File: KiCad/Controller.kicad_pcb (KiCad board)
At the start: 2 copper layers, 45 x 45 mm, 37 parts, among them J1 Inputs, J2 POWER, J3 RANGER, J4 RFID, J5 OUT1, J6 OUT2, J7 OUT3, J8 OUT4, J9 USB-C, M1 D24V5F3-NoSHDN, M2 D24V5F5-NoSHDN, Q1 BC817, U1 ESP32-WROOM-32, U2 G3VM-41GR8, U3 G3VM-41GR8, U4 G3VM-41GR8, U5 G3VM-41GR8, U6 FT231XQ, U7 QR

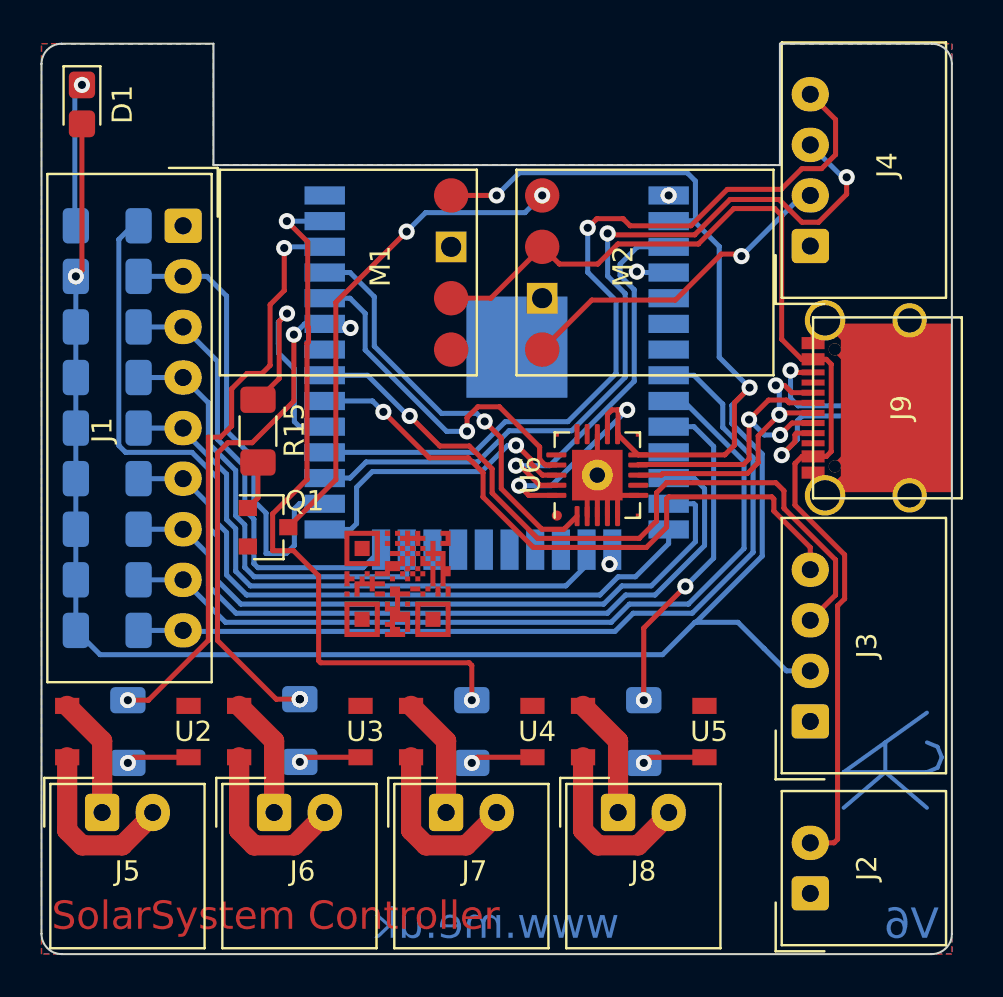
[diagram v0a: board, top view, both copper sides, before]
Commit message: Updated QR, and added 3D (not finished)
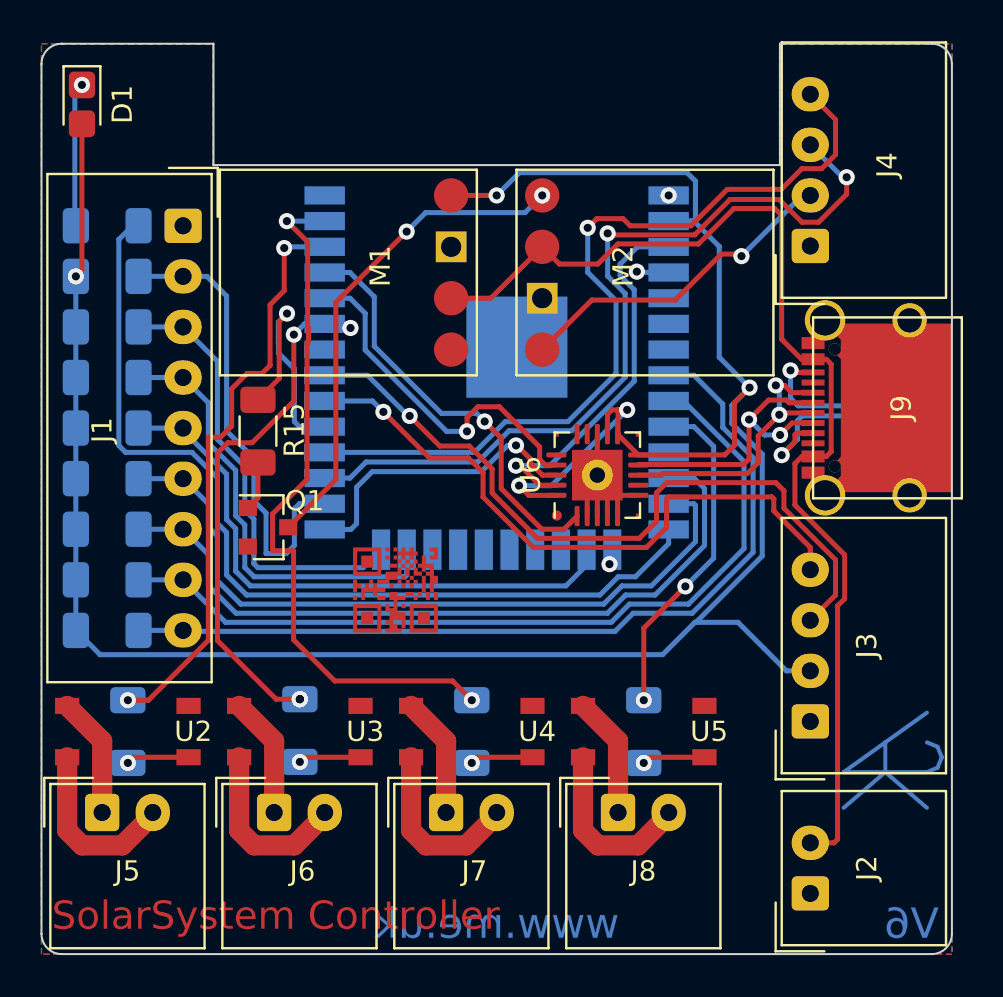
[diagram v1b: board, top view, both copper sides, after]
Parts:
- moved U7 0.32 mm to (67.5, 122.0)
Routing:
- net OUT3: track 35.7 -> 34.8 mm

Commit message: New regulator
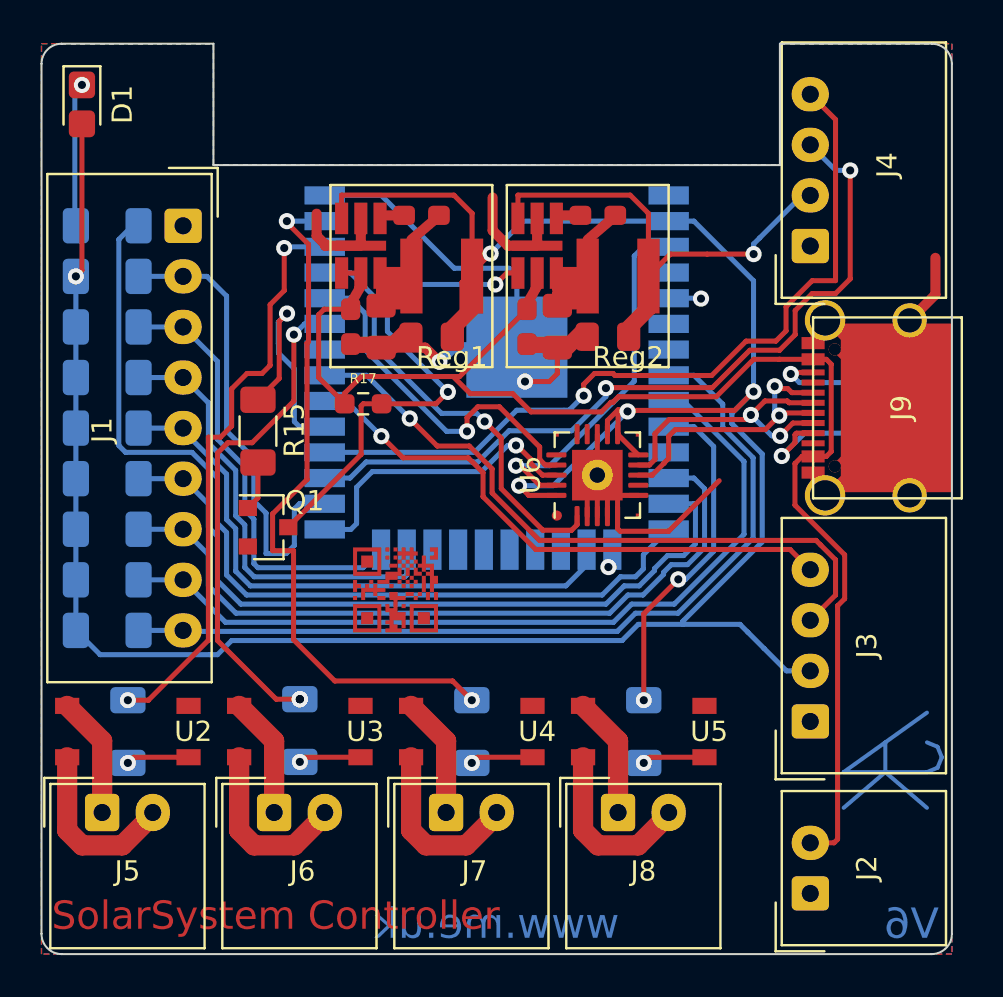
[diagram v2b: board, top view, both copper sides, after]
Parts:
- removed M1: D24V5F3-NoSHDN, RevK:D24V5F3-SMD-Like
- removed M2: D24V5F5-NoSHDN, RevK:D24V5F3-SMD-Like
- added R17: 100K, Resistor_SMD:R_0603_1608Metric_Pad0.98x0.95mm_HandSolder, F.Cu at (65.9, 112.8)
- added Reg1: Regulator, RevK:RegulatorBlock, F.Cu at (65.8, 105.0)
- added Reg2: Regulator, RevK:RegulatorBlock, F.Cu at (74.5, 105.0)
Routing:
- net GND: track 46.2 -> 100.5 mm, vias 3 -> 4
- net VBUS: track 55.6 -> 70.9 mm
- net SDA: track 32.0 -> 28.2 mm
- net SCL: track 36.8 -> 33.2 mm
- net +5V: track 16.5 -> 13.3 mm
- net +3V3: track 125.9 -> 123.1 mm
- net RFRX: track 41.3 -> 38.9 mm
- net Net-(J9-PadB5): track 7.07 -> 5.02 mm
- net RFTX: track 41.3 -> 39.6 mm
- net OUT2: track 25.9 -> 24.4 mm, vias 4 -> 3
- net Net-(J9-PadA5): track 8.07 -> 6.88 mm
- net EN: track 18.8 -> 18.1 mm
- net Net-(Q1-Pad3): track 24.5 -> 25.1 mm

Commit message: Yet more component tweaks
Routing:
- net GND: track 100.5 -> 107.4 mm, vias 4 -> 5
- net +3V3: track 123.1 -> 126.3 mm
- net +5V: track 13.3 -> 16.1 mm
- net VBUS: track 70.9 -> 71.5 mm

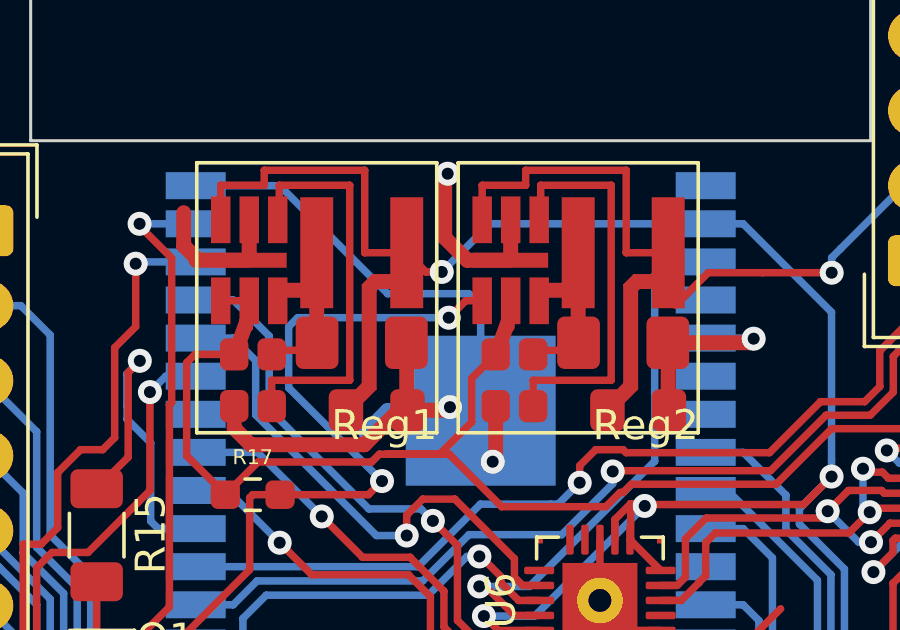
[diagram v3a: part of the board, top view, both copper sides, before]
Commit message: Cleaner regulator layout
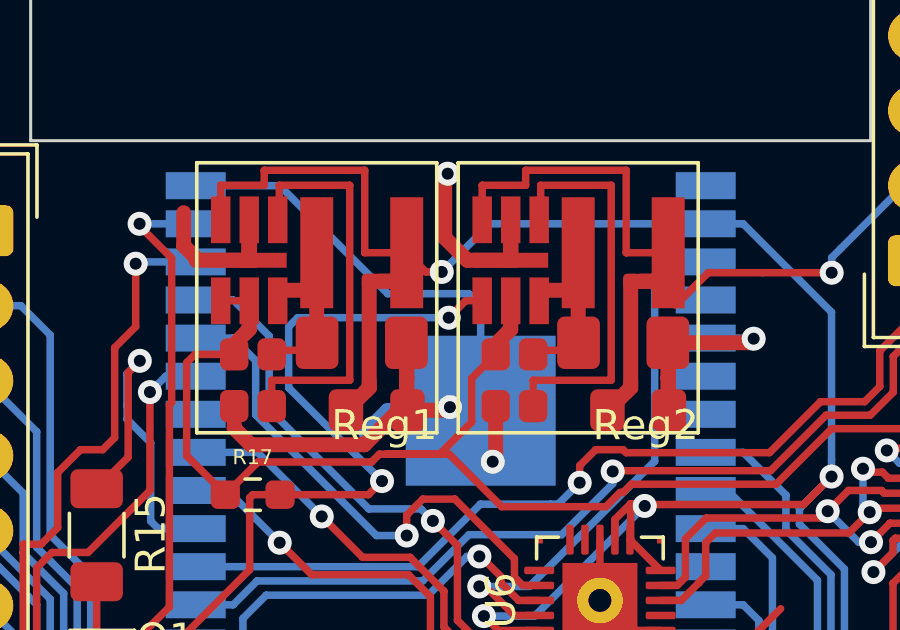
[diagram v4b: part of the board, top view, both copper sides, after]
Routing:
- net GND: track 107.4 -> 101.4 mm
- net +3V3: track 126.3 -> 120.5 mm
- net +5V: track 16.1 -> 10.9 mm
- net VBUS: track 71.5 -> 67.5 mm

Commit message: Yet more tweaks!
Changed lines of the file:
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@@
       (effects (font (size 1 1) (thickness 0.15)))
     )
+    (fp_line (start 0.75 4.75) (end 0.75 4) (layer F.Cu) (width 0.25))
+    (fp_line (start 0.5 -3) (end 3.85 -3) (layer F.Cu) (width 0.25))
+    (fp_line (start -0.95 -1.3) (end -0.95 -2.5) (layer F.Cu) (width 0.25))
+    (fp_line (start 1 -2.5) (end 3.35 -2.5) (layer F.Cu) (width 0.25))
+    (fp_line (start 1 -1.3) (end 1 -2.5) (layer F.Cu) (width 0.25))
+    (fp_line (start 3.35 4) (end 3.35 -2.5) (layer F.Cu) (width 0.25))
+    (fp_line (start 0.75 4) (end 3.35 4) (layer F.Cu) (width 0.25))
+    (fp_line (start 2.25 3) (end 0.75 3) (layer F.Cu) (width 0.25))
+    (fp_line (start 2.25 1) (end 2.25 3) (layer F.Cu) (width 0.5))
+    (fp_line (start 2.4 1) (end 1 1) (layer F.Cu) (width 0.5))
+    (fp_line (start -1.75 5.75) (end -1.75 -3.25) (layer F.Fab) (width 0.12))
+    (fp_line (start 6.25 5.75) (end -1.75 5.75) (layer F.Fab) (width 0.12))
+    (fp_line (start 6.25 -3.25) (end 6.25 5.75) (layer F.Fab) (width 0.12))
+    (fp_line (start -1.75 -3.25) (end 6.25 -3.25) (layer F.Fab) (width 0.12))
+    (fp_line (start -1.75 5.75) (end -1.75 -3.25) (layer F.CrtYd) (width 0.12))
+    (fp_line (start 6.25 5.75) (end -1.75 5.75) (layer F.CrtYd) (width 0.12))
+    (fp_line (start 6.25 -3.25) (end 6.25 5.75) (layer F.CrtYd) (width 0.12))
+    (fp_line (start -1.75 -3.25) (end 6.25 -3.25) (layer F.CrtYd) (width 0.12))
+    (fp_line (start -1.75 5.75) (end -1.75 -3.25) (layer F.SilkS) (width 0.12))
+    (fp_line (start 6.25 5.75) (end -1.75 5.75) (layer F.SilkS) (width 0.12))
+    (fp_line (start 6.25 -3.25) (end 6.25 5.75) (layer F.SilkS) (width 0.12))
+    (fp_line (start -1.75 -3.25) (end 6.25 -3.25) (layer F.SilkS) (width 0.12))
+    (fp_line (start 3.85 -0.25) (end 3.85 -3) (layer F.Cu) (width 0.25))
+    (fp_line (start 3.85 -0.25) (end 4.7 -0.25) (layer F.Cu) (width 0.25))
+    (fp_line (start 0.5 -2.5) (end 0.5 -3) (layer F.Cu) (width 0.25))
     (fp_line (start 0.5 -2.5) (end -0.95 -2.5) (layer F.Cu) (width 0.25))
-    (fp_line (start 0.5 -2.5) (end 0.5 -3) (layer F.Cu) (width 0.25))
-    (fp_line (start 3.85 -0.25) (end 4.7 -0.25) (layer F.Cu) (width 0.25))
-    (fp_line (start 3.85 -0.25) (end 3.85 -3) (layer F.Cu) (width 0.25))
-    (fp_line (start -1.75 -3.25) (end 6.25 -3.25) (layer F.SilkS) (width 0.12))
-    (fp_line (start 6.25 -3.25) (end 6.25 5.75) (layer F.SilkS) (width 0.12))
-    (fp_line (start 6.25 5.75) (end -1.75 5.75) (layer F.SilkS) (width 0.12))
-    (fp_line (start -1.75 5.75) (end -1.75 -3.25) (layer F.SilkS) (width 0.12))
-    (fp_line (start -1.75 -3.25) (end 6.25 -3.25) (layer F.CrtYd) (width 0.12))
-    (fp_line (start 6.25 -3.25) (end 6.25 5.75) (layer F.CrtYd) (width 0.12))
-    (fp_line (start 6.25 5.75) (end -1.75 5.75) (layer F.CrtYd) (width 0.12))
-    (fp_line (start -1.75 5.75) (end -1.75 -3.25) (layer F.CrtYd) (width 0.12))
-    (fp_line (start -1.75 -3.25) (end 6.25 -3.25) (layer F.Fab) (width 0.12))
-    (fp_line (start 6.25 -3.25) (end 6.25 5.75) (layer F.Fab) (width 0.12))
-    (fp_line (start 6.25 5.75) (end -1.75 5.75) (layer F.Fab) (width 0.12))
-    (fp_line (start -1.75 5.75) (end -1.75 -3.25) (layer F.Fab) (width 0.12))
-    (fp_line (start 2.4 1) (end 1 1) (layer F.Cu) (width 0.5))
-    (fp_line (start 2.25 1) (end 2.25 3) (layer F.Cu) (width 0.5))
-    (fp_line (start 2.25 3) (end 0.75 3) (layer F.Cu) (width 0.25))
-    (fp_line (start 0.75 4) (end 3.35 4) (layer F.Cu) (width 0.25))
-    (fp_line (start 3.35 4) (end 3.35 -2.5) (layer F.Cu) (width 0.25))
-    (fp_line (start 1 -1.3) (end 1 -2.5) (layer F.Cu) (width 0.25))
-    (fp_line (start 1 -2.5) (end 3.35 -2.5) (layer F.Cu) (width 0.25))
-    (fp_line (start -0.95 -1.3) (end -0.95 -2.5) (layer F.Cu) (width 0.25))
-    (fp_line (start 0.5 -3) (end 3.85 -3) (layer F.Cu) (width 0.25))
-    (fp_line (start 0.75 4.75) (end 0.75 4) (layer F.Cu) (width 0.25))
     (pad 4 smd rect (at 4.8 0.7 90) (size 0.5 1) (layers F.Cu)
       (net 17 +5V) (zone_connect 0))
@@
     (pad 2 smd rect (at 0 1.85) (size 0.5 1) (layers F.Cu)
       (net 18 VBUS) (zone_connect 0))
-    (pad 2 smd rect (at -0.3 2.6 135) (size 0.5 1) (layers F.Cu)
+    (pad 2 smd rect (at -0.35 2.65 135) (size 0.5 1) (layers F.Cu)
       (net 18 VBUS) (zone_connect 0))
     (pad 3 smd rect (at 5.25 4.35) (size 0.5 1) (layers F.Cu)
@@
       (effects (font (size 1 1) (thickness 0.15)))
     )
+    (fp_line (start 0.75 4.75) (end 0.75 4) (layer F.Cu) (width 0.25))
+    (fp_line (start 0.5 -3) (end 3.85 -3) (layer F.Cu) (width 0.25))
+    (fp_line (start -0.95 -1.3) (end -0.95 -2.5) (layer F.Cu) (width 0.25))
+    (fp_line (start 1 -2.5) (end 3.35 -2.5) (layer F.Cu) (width 0.25))
+    (fp_line (start 1 -1.3) (end 1 -2.5) (layer F.Cu) (width 0.25))
+    (fp_line (start 3.35 4) (end 3.35 -2.5) (layer F.Cu) (width 0.25))
+    (fp_line (start 0.75 4) (end 3.35 4) (layer F.Cu) (width 0.25))
+    (fp_line (start 2.25 3) (end 0.75 3) (layer F.Cu) (width 0.25))
+    (fp_line (start 2.25 1) (end 2.25 3) (layer F.Cu) (width 0.5))
+    (fp_line (start 2.4 1) (end 1 1) (layer F.Cu) (width 0.5))
+    (fp_line (start -1.75 5.75) (end -1.75 -3.25) (layer F.Fab) (width 0.12))
+    (fp_line (start 6.25 5.75) (end -1.75 5.75) (layer F.Fab) (width 0.12))
+    (fp_line (start 6.25 -3.25) (end 6.25 5.75) (layer F.Fab) (width 0.12))
+    (fp_line (start -1.75 -3.25) (end 6.25 -3.25) (layer F.Fab) (width 0.12))
+    (fp_line (start -1.75 5.75) (end -1.75 -3.25) (layer F.CrtYd) (width 0.12))
+    (fp_line (start 6.25 5.75) (end -1.75 5.75) (layer F.CrtYd) (width 0.12))
+    (fp_line (start 6.25 -3.25) (end 6.25 5.75) (layer F.CrtYd) (width 0.12))
+    (fp_line (start -1.75 -3.25) (end 6.25 -3.25) (layer F.CrtYd) (width 0.12))
+    (fp_line (start -1.75 5.75) (end -1.75 -3.25) (layer F.SilkS) (width 0.12))
+    (fp_line (start 6.25 5.75) (end -1.75 5.75) (layer F.SilkS) (width 0.12))
+    (fp_line (start 6.25 -3.25) (end 6.25 5.75) (layer F.SilkS) (width 0.12))
+    (fp_line (start -1.75 -3.25) (end 6.25 -3.25) (layer F.SilkS) (width 0.12))
+    (fp_line (start 3.85 -0.25) (end 3.85 -3) (layer F.Cu) (width 0.25))
+    (fp_line (start 3.85 -0.25) (end 4.7 -0.25) (layer F.Cu) (width 0.25))
+    (fp_line (start 0.5 -2.5) (end 0.5 -3) (layer F.Cu) (width 0.25))
     (fp_line (start 0.5 -2.5) (end -0.95 -2.5) (layer F.Cu) (width 0.25))
-    (fp_line (start 0.5 -2.5) (end 0.5 -3) (layer F.Cu) (width 0.25))
-    (fp_line (start 3.85 -0.25) (end 4.7 -0.25) (layer F.Cu) (width 0.25))
-    (fp_line (start 3.85 -0.25) (end 3.85 -3) (layer F.Cu) (width 0.25))
-    (fp_line (start -1.75 -3.25) (end 6.25 -3.25) (layer F.SilkS) (width 0.12))
-    (fp_line (start 6.25 -3.25) (end 6.25 5.75) (layer F.SilkS) (width 0.12))
-    (fp_line (start 6.25 5.75) (end -1.75 5.75) (layer F.SilkS) (width 0.12))
-    (fp_line (start -1.75 5.75) (end -1.75 -3.25) (layer F.SilkS) (width 0.12))
-    (fp_line (start -1.75 -3.25) (end 6.25 -3.25) (layer F.CrtYd) (width 0.12))
-    (fp_line (start 6.25 -3.25) (end 6.25 5.75) (layer F.CrtYd) (width 0.12))
-    (fp_line (start 6.25 5.75) (end -1.75 5.75) (layer F.CrtYd) (width 0.12))
-    (fp_line (start -1.75 5.75) (end -1.75 -3.25) (layer F.CrtYd) (width 0.12))
-    (fp_line (start -1.75 -3.25) (end 6.25 -3.25) (layer F.Fab) (width 0.12))
-    (fp_line (start 6.25 -3.25) (end 6.25 5.75) (layer F.Fab) (width 0.12))
-    (fp_line (start 6.25 5.75) (end -1.75 5.75) (layer F.Fab) (width 0.12))
-    (fp_line (start -1.75 5.75) (end -1.75 -3.25) (layer F.Fab) (width 0.12))
-    (fp_line (start 2.4 1) (end 1 1) (layer F.Cu) (width 0.5))
-    (fp_line (start 2.25 1) (end 2.25 3) (layer F.Cu) (width 0.5))
-    (fp_line (start 2.25 3) (end 0.75 3) (layer F.Cu) (width 0.25))
-    (fp_line (start 0.75 4) (end 3.35 4) (layer F.Cu) (width 0.25))
-    (fp_line (start 3.35 4) (end 3.35 -2.5) (layer F.Cu) (width 0.25))
-    (fp_line (start 1 -1.3) (end 1 -2.5) (layer F.Cu) (width 0.25))
-    (fp_line (start 1 -2.5) (end 3.35 -2.5) (layer F.Cu) (width 0.25))
-    (fp_line (start -0.95 -1.3) (end -0.95 -2.5) (layer F.Cu) (width 0.25))
-    (fp_line (start 0.5 -3) (end 3.85 -3) (layer F.Cu) (width 0.25))
-    (fp_line (start 0.75 4.75) (end 0.75 4) (layer F.Cu) (width 0.25))
     (pad 4 smd rect (at 4.8 0.7 90) (size 0.5 1) (layers F.Cu)
       (net 14 +3V3) (zone_connect 0))
@@
     (pad 2 smd rect (at 0 1.85) (size 0.5 1) (layers F.Cu)
       (net 18 VBUS) (zone_connect 0))
-    (pad 2 smd rect (at -0.3 2.6 135) (size 0.5 1) (layers F.Cu)
+    (pad 2 smd rect (at -0.35 2.65 135) (size 0.5 1) (layers F.Cu)
       (net 18 VBUS) (zone_connect 0))
     (pad 3 smd rect (at 5.25 4.35) (size 0.5 1) (layers F.Cu)

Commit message: More updates
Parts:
- removed R13, R14: 5K1, Resistor_SMD:R_1206_3216Metric_Pad1.30x1.75mm_HandSolder
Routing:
- net GND: track 101.4 -> 69.5 mm

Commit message: 0603
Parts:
- added R13: 5K1, Resistor_SMD:R_0603_1608Metric_Pad0.98x0.95mm_HandSolder, B.Cu at (91.8, 114.5)
- added R14: 5K1, Resistor_SMD:R_0603_1608Metric_Pad0.98x0.95mm_HandSolder, B.Cu at (91.8, 111.2)
- D1: footprint LED_SMD:LED_0805_2012Metric_Castellated -> LED_SMD:LED_0603_1608Metric_Pad1.05x0.95mm_HandSolder
- R15, R16, R3, R4, R5, R6: footprint Resistor_SMD:R_1206_3216Metric_Pad1.30x1.75mm_HandSolder -> Resistor_SMD:R_0603_1608Metric_Pad0.98x0.95mm_HandSolder
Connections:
- U1 pad 4: GND -> Net-(U1-Pad4)
- U1 pad 5: GND -> Net-(U1-Pad5)
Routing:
- net IN1: track 23.3 -> 19.0 mm
- net GND: track 69.5 -> 67.9 mm, vias 5 -> 4
- net IN7: track 41.2 -> 40.3 mm
- net IN8: track 43.5 -> 42.6 mm
- net Net-(Q1-Pad3): track 25.4 -> 26.1 mm
- net Net-(D1-Pad1): track 7.11 -> 7.79 mm
- net Net-(R6-Pad1): track 3.12 -> 3.75 mm
- net Net-(R5-Pad1): track 3.12 -> 3.75 mm
- net Net-(R3-Pad1): track 3.12 -> 3.75 mm
- net SHDN: track 12.3 -> 12.9 mm
- net OUT4: track 16.8 -> 17.5 mm
- net Net-(Q1-Pad1): track 2.46 -> 3.09 mm
- net OUT3: track 34.8 -> 35.5 mm
- net Net-(R4-Pad1): track 3.10 -> 3.73 mm
- net LED: track 46.1 -> 45.5 mm
